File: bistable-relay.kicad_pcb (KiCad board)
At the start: 2 copper layers, 21.2 x 11.1 mm, 9 parts, among them J1 edge_connector, K1 FH44L-1AT-L1-DC5V, U1 MIC4427

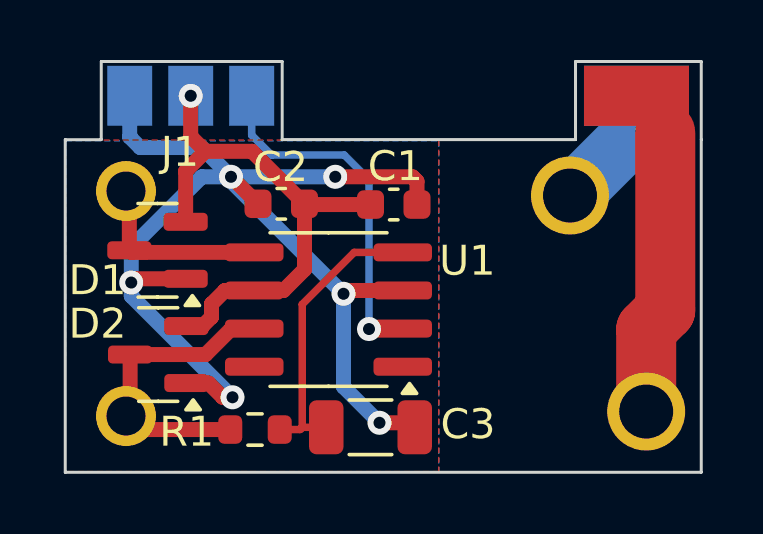
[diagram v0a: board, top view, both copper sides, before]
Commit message: change 100nF capacitor to 0402 package
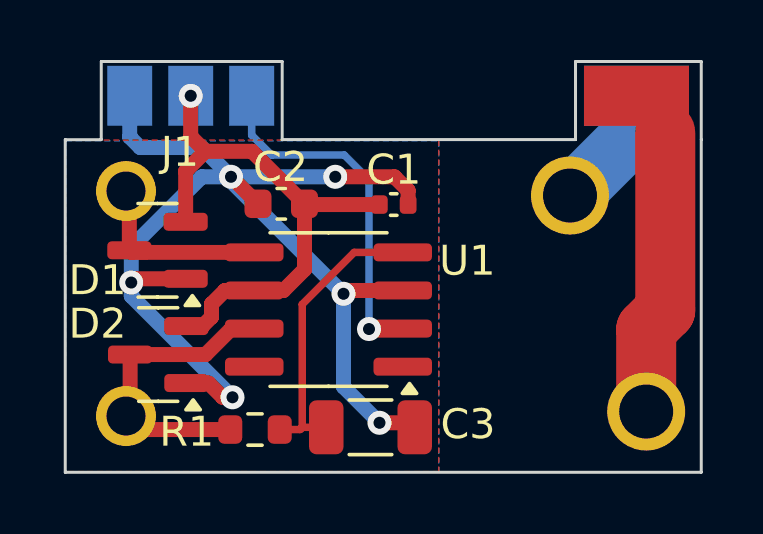
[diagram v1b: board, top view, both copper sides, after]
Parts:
- C1: footprint Capacitor_SMD:C_0603_1608Metric -> Capacitor_SMD:C_0402_1005Metric
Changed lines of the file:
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@@
 		)
 	)
-	(footprint "Capacitor_SMD:C_0603_1608Metric"
+	(footprint "Capacitor_SMD:C_0402_1005Metric"
 		(layer "F.Cu")
 		(at 140.825 97.125)
-		(descr "Capacitor SMD 0603 (1608 Metric), square (rectangular) end terminal, IPC_7351 nominal, (Body size source: IPC-SM-782 page 76, https://www.pcb-3d.com/wordpress/wp-content/uploads/ipc-sm-782a_amendment_1_and_2.pdf), generated with kicad-footprint-generator")
+		(descr "Capacitor SMD 0402 (1005 Metric), square (rectangular) end terminal, IPC_7351 nominal, (Body size source: IPC-SM-782 page 76, https://www.pcb-3d.com/wordpress/wp-content/uploads/ipc-sm-782a_amendment_1_and_2.pdf), generated with kicad-footprint-generator")
 		(tags "capacitor")
 		(property "Reference" "C1"
-			(at 0.05 -1.275 0)
+			(at 0 -1.16 0)
 			(layer "F.SilkS")
 			(effects
@@
 		)
 		(property "Value" "100n"
-			(at 0 1.43 0)
+			(at 0 1.16 0)
 			(layer "F.Fab")
 			(effects
@@
 			)
 		)
-		(property "Footprint" "Capacitor_SMD:C_0603_1608Metric"
+		(property "Footprint" "Capacitor_SMD:C_0402_1005Metric"
 			(at 0 0 0)
+			(unlocked yes)
 			(layer "F.Fab")
 			(hide yes)
@@
 		(property "Datasheet" ""
 			(at 0 0 0)
+			(unlocked yes)
 			(layer "F.Fab")
 			(hide yes)
@@
 		(property "Description" ""
 			(at 0 0 0)
+			(unlocked yes)
 			(layer "F.Fab")
 			(hide yes)
@@
 		(attr smd)
 		(fp_line
-			(start -0.14058 -0.51)
-			(end 0.14058 -0.51)
+			(start -0.107836 -0.36)
+			(end 0.107836 -0.36)
 			(stroke
 				(width 0.12)
@@
 		)
 		(fp_line
-			(start -0.14058 0.51)
-			(end 0.14058 0.51)
+			(start -0.107836 0.36)
+			(end 0.107836 0.36)
 			(stroke
 				(width 0.12)
@@
 		)
 		(fp_line
-			(start -1.48 -0.73)
-			(end 1.48 -0.73)
+			(start -0.91 -0.46)
+			(end 0.91 -0.46)
 			(stroke
 				(width 0.05)
@@
 		)
 		(fp_line
-			(start -1.48 0.73)
-			(end -1.48 -0.73)
+			(start -0.91 0.46)
+			(end -0.91 -0.46)
 			(stroke
 				(width 0.05)
@@
 		)
 		(fp_line
-			(start 1.48 -0.73)
-			(end 1.48 0.73)
+			(start 0.91 -0.46)
+			(end 0.91 0.46)
 			(stroke
 				(width 0.05)
@@
 		)
 		(fp_line
-			(start 1.48 0.73)
-			(end -1.48 0.73)
+			(start 0.91 0.46)
+			(end -0.91 0.46)
 			(stroke
 				(width 0.05)
@@
 		)
 		(fp_line
-			(start -0.8 -0.4)
-			(end 0.8 -0.4)
+			(start -0.5 -0.25)
+			(end 0.5 -0.25)
 			(stroke
 				(width 0.1)
@@
 		)
 		(fp_line
-			(start -0.8 0.4)
-			(end -0.8 -0.4)
+			(start -0.5 0.25)
+			(end -0.5 -0.25)
 			(stroke
 				(width 0.1)
@@
 		)
 		(fp_line
-			(start 0.8 -0.4)
-			(end 0.8 0.4)
+			(start 0.5 -0.25)
+			(end 0.5 0.25)
 			(stroke
 				(width 0.1)
@@
 		)
 		(fp_line
-			(start 0.8 0.4)
-			(end -0.8 0.4)
+			(start 0.5 0.25)
+			(end -0.5 0.25)
 			(stroke
 				(width 0.1)
@@
 			(effects
 				(font
-					(size 0.4 0.4)
-					(thickness 0.06)
+					(size 0.25 0.25)
+					(thickness 0.04)
 				)
 			)
 		)
 		(pad "1" smd roundrect
-			(at -0.775 0)
-			(size 0.9 0.95)
+			(at -0.48 0)
+			(size 0.56 0.62)
 			(layers "F.Cu" "F.Paste" "F.Mask")
 			(roundrect_rratio 0.25)
@@
 		)
 		(pad "2" smd roundrect
-			(at 0.775 0)
-			(size 0.9 0.95)
+			(at 0.48 0)
+			(size 0.56 0.62)
 			(layers "F.Cu" "F.Paste" "F.Mask")
 			(roundrect_rratio 0.25)
@@
 			(pintype "passive")
 		)
-		(model "${KICAD6_3DMODEL_DIR}/Capacitor_SMD.3dshapes/C_0603_1608Metric.wrl"
+		(model "${KICAD8_3DMODEL_DIR}/Capacitor_SMD.3dshapes/C_0402_1005Metric.wrl"
 			(offset
 				(xyz 0 0 0)
@@
 	)
 	(segment
+		(start 140.345 97.125)
+		(end 137.875 97.125)
+		(width 0.5)
+		(layer "F.Cu")
+		(net 1)
+	)
+	(segment
 		(start 136.175 99.99)
 		(end 137.149999 99.99)
@@
 	)
 	(segment
+		(start 137.875 97.125)
+		(end 137.85 97.1)
+		(width 0.5)
+		(layer "F.Cu")
+		(net 1)
+	)
+	(segment
 		(start 135.200001 99.99)
 		(end 136.175 99.99)
@@
 		(start 133.8875 96.0125)
 		(end 133.8875 97.7)
-		(width 0.5)
-		(layer "F.Cu")
-		(net 1)
-	)
-	(segment
-		(start 140.05 97.125)
-		(end 137.875 97.125)
-		(width 0.5)
-		(layer "F.Cu")
-		(net 1)
-	)
-	(segment
-		(start 137.875 97.125)
-		(end 137.85 97.1)
 		(width 0.5)
 		(layer "F.Cu")
@@
 	)
 	(segment
+		(start 138.875 96.2)
+		(end 140.85 96.2)
+		(width 0.5)
+		(layer "F.Cu")
+		(net 2)
+	)
+	(segment
 		(start 140.35 104.4)
 		(end 141.375 104.4)
@@
 	)
 	(segment
-		(start 138.875 96.2)
-		(end 141.45 96.2)
-		(width 0.5)
-		(layer "F.Cu")
-		(net 2)
-	)
-	(segment
 		(start 134.65 103.075)
 		(end 135.125 103.55)
@@
 	)
 	(segment
+		(start 140.85 96.2)
+		(end 141.305 96.655)
+		(width 0.5)
+		(layer "F.Cu")
+		(net 2)
+	)
+	(segment
 		(start 133.8875 99.6)
 		(end 132.2 99.6)
@@
 	)
 	(segment
-		(start 141.6 96.35)
-		(end 141.6 97.125)
-		(width 0.5)
-		(layer "F.Cu")
-		(net 2)
-	)
-	(segment
 		(start 141.375 104.4)
 		(end 141.525 104.55)
@@
 	)
 	(segment
+		(start 141.305 96.655)
+		(end 141.305 97.125)
+		(width 0.5)
+		(layer "F.Cu")
+		(net 2)
+	)
+	(segment
 		(start 132.2 99.6)
 		(end 132.075 99.725)
@@
 		(width 0.5)
 		(layer "F.Cu")
-		(net 2)
-	)
-	(segment
-		(start 141.45 96.2)
-		(end 141.6 96.35)
-		(width 0.5)
-		(layer "F.Cu")
